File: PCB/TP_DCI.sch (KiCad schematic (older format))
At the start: 56 parts, among them K1 G5V-2-5DC, K2 G5V-2-5DC, P1 Conn_02x20, P2 Conn_02x20, Q1 BC817W, Q2 BC817W, U1 PS2805-4, U2 ACS725xLCTR-10AU, U3 PS2805-4, U4 ACS725xLCTR-10AU, U5 24AA1025, U6 DS3231

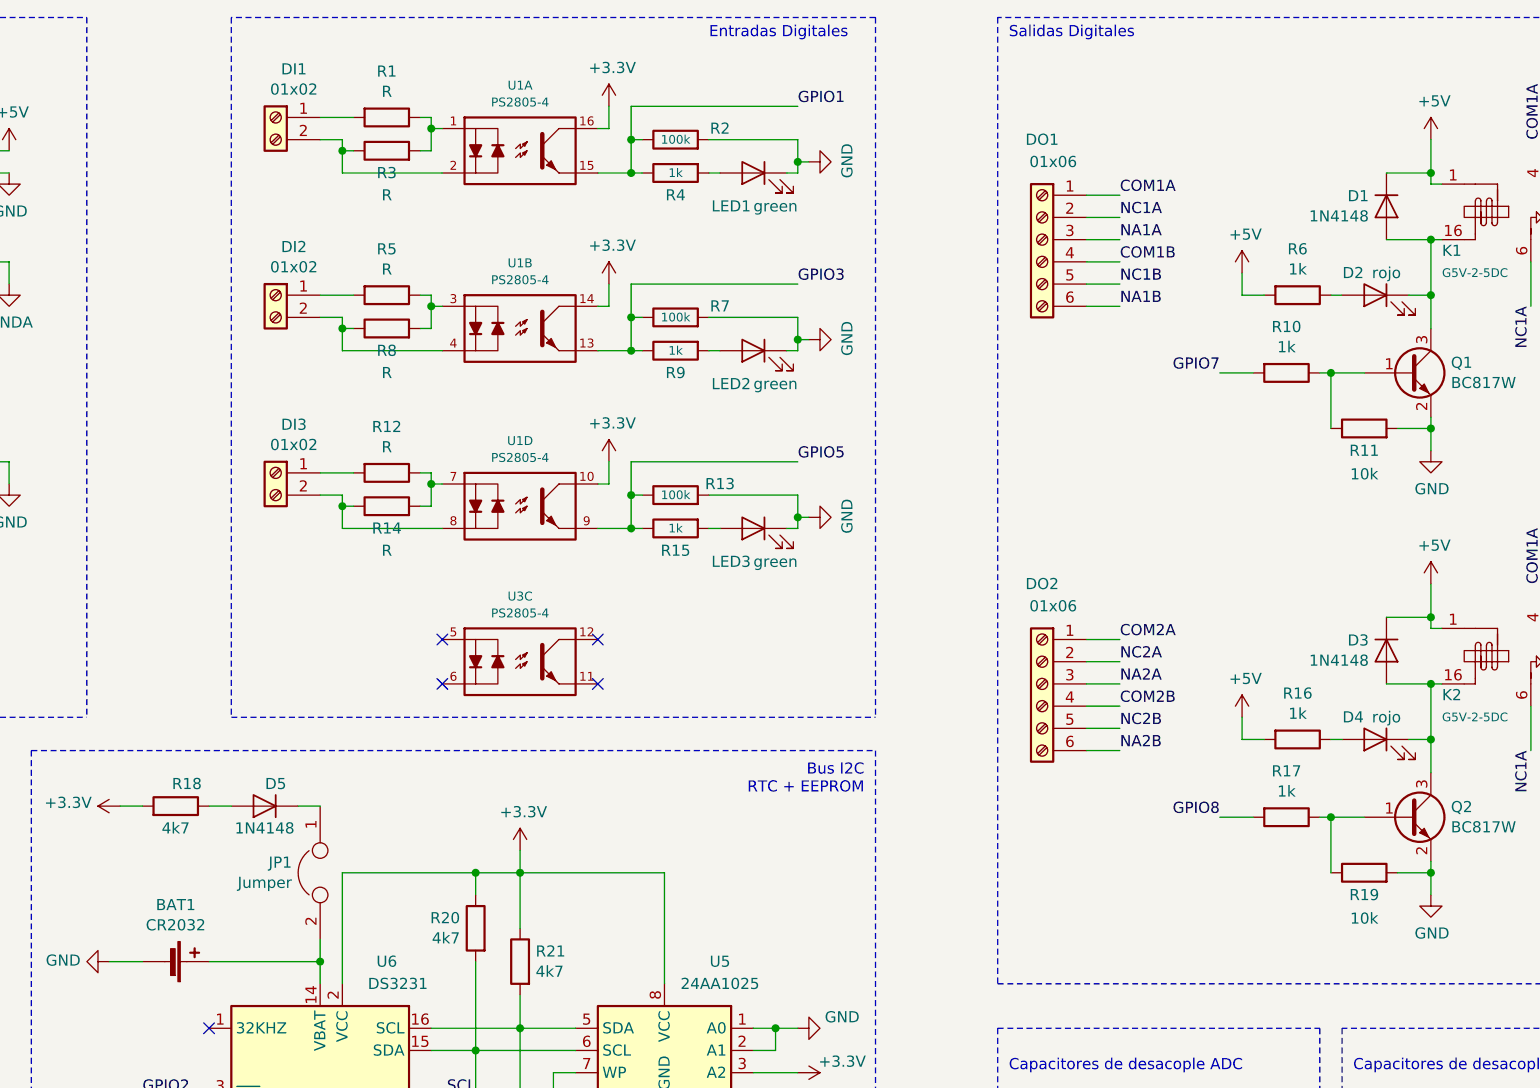
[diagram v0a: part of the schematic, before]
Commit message: correccion de footprints
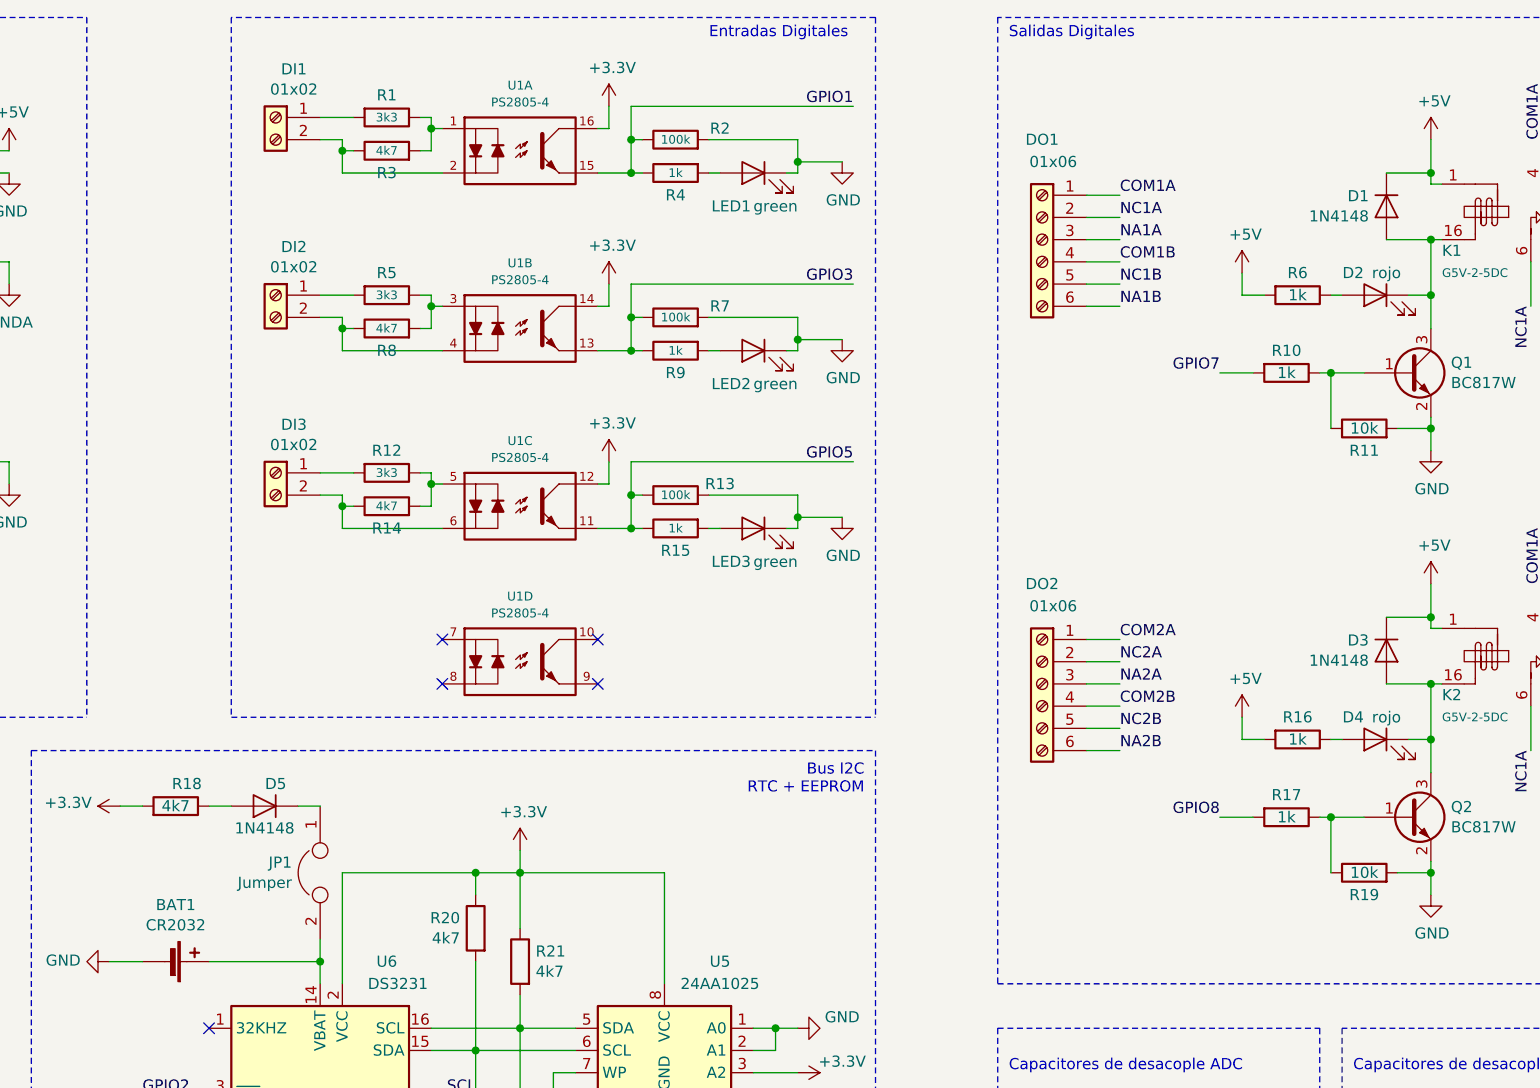
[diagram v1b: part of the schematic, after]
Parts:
- DO1, DO2: footprint (none) -> TerminalBlock:TerminalBlock_bornier-6_P5.08mm
- P1, P2: footprint Connector_IDC:IDC-Header_2x20_P2.54mm_Horizontal -> Connector_PinHeader_1.27mm:PinHeader_2x20_P1.27mm_Vertical
- R1, R12, R5: value R -> 3k3; footprint (none) -> Resistor_SMD:R_0805_2012Metric
- R10, R11, R13, R15, R16, R17, R18, R19, R2, R20, R21, R4, R6, R7, R9: footprint (none) -> Resistor_SMD:R_0805_2012Metric
- R14, R3, R8: value R -> 4k7; footprint (none) -> Resistor_SMD:R_0805_2012Metric
- U1: footprint SSOP-16 -> Package_SO:SOP-16_4.4x10.4mm_P1.27mm
- U1: renamed from U3; footprint SSOP-16 -> Package_SO:SOP-16_4.4x10.4mm_P1.27mm
- U5: footprint (none) -> Package_SO:SOIC-8_5.23x5.23mm_P1.27mm
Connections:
- net +3V3: now also U1.12; no longer U1.10
- net GPIO5: now also U1.11; no longer U1.9
- net at DI3.2 (Pin_2), R14.1: now also U1.6; no longer U1.8
- net at R12.1, R14.2: now also U1.5; no longer U1.7

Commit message: Se incorpora plantilla de poncho EDU-CIAA
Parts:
- DO2: footprint TerminalBlock:TerminalBlock_bornier-6_P5.08mm -> Connector_PinHeader_2.54mm:PinHeader_2x03_P2.54mm_Vertical; symbol Connector:Screw_Terminal_01x06 -> Connector_Generic:Conn_02x03_Odd_Even
- P1, P2: footprint Connector_PinHeader_1.27mm:PinHeader_2x20_P1.27mm_Vertical -> Connector_PinHeader_2.54mm:PinHeader_2x20_P2.54mm_Vertical
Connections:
- net COM1B: now also DO2.4 (Pin_4); no longer DO1.4 (Pin_4)
- net COM2A: now also DO1.4 (Pin_4); no longer DO2.1 (Pin_1)
- net COM2B: now also DO2.1 (Pin_1); no longer DO2.4 (Pin_4)
- net NA1B: now also DO2.6 (Pin_6); no longer DO1.6 (Pin_6)
- net NA2A: now also DO1.6 (Pin_6); no longer DO2.3 (Pin_3)
- net NA2B: now also DO2.3 (Pin_3); no longer DO2.6 (Pin_6)
- net NC1B: now also DO2.5 (Pin_5); no longer DO1.5 (Pin_5)
- net NC2A: now also DO1.5 (Pin_5); no longer DO2.2 (Pin_2)
- net NC2B: now also DO2.2 (Pin_2); no longer DO2.5 (Pin_5)
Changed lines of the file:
@@
 Wire Wire Line
 	8400 1750 8550 1750
+Text Label 8350 3100 2    50   ~ 0
+COM1B
+Wire Wire Line
+	8400 1850 8550 1850
+Text Label 9150 3200 0    50   ~ 0
+NC1B
+Wire Wire Line
+	8400 1950 8550 1950
+Text Label 8350 3200 2    50   ~ 0
+NA1B
 Text Label 8550 1750 0    50   ~ 0
-COM1B
-Wire Wire Line
-	8400 1850 8550 1850
+COM2A
+Wire Wire Line
+	8350 3100 8500 3100
 Text Label 8550 1850 0    50   ~ 0
-NC1B
-Wire Wire Line
-	8400 1950 8550 1950
+NC2A
+Wire Wire Line
+	8350 3200 8500 3200
 Text Label 8550 1950 0    50   ~ 0
-NA1B
-Wire Wire Line
-	8400 3450 8550 3450
-Text Label 8550 3450 0    50   ~ 0
-COM2A
-Wire Wire Line
-	8400 3550 8550 3550
-Text Label 8550 3550 0    50   ~ 0
-NC2A
-Wire Wire Line
-	8400 3650 8550 3650
-Text Label 8550 3650 0    50   ~ 0
 NA2A
 Wire Wire Line
-	8400 3750 8550 3750
-Text Label 8550 3750 0    50   ~ 0
+	9000 3000 9150 3000
+Text Label 9150 3000 0    50   ~ 0
 COM2B
 Wire Wire Line
-	8400 3850 8550 3850
-Text Label 8550 3850 0    50   ~ 0
+	9000 3100 9150 3100
+Text Label 8350 3000 2    50   ~ 0
 NC2B
 Wire Wire Line
-	8400 3950 8550 3950
-Text Label 8550 3950 0    50   ~ 0
+	9000 3200 9150 3200
+Text Label 9150 3100 0    50   ~ 0
 NA2B
 Wire Wire Line
@@
 	9950 1350 9950 1400
 $Comp
-L Connector:Screw_Terminal_01x06 DO2
+L Connector_Generic:Conn_02x03_Odd_Even DO2
 U 1 1 61C48A0E
-P 8200 3650
-F 0 "DO2" H 8200 4100 50  0000 C CNN
-F 1 "01x06" H 8150 4000 50  0000 C CNN
-F 2 "TerminalBlock:TerminalBlock_bornier-6_P5.08mm" H 8200 3650 50  0001 C CNN
-F 3 "~" H 8200 3650 50  0001 C CNN
-	1    8200 3650
+P 8800 3100
+F 0 "DO2" H 8850 3417 50  0000 C CNN
+F 1 "01x06" H 8850 3326 50  0000 C CNN
+F 2 "Connector_PinHeader_2.54mm:PinHeader_2x03_P2.54mm_Vertical" H 8800 3100 50  0001 C CNN
+F 3 "~" H 8800 3100 50  0001 C CNN
+	1    8800 3100
 	-1   0    0    -1
 $EndComp
@@
 F 0 "P1" H 1450 3267 50  0000 C CNN
 F 1 "Conn_02x20" H 1450 3176 50  0000 C CNN
-F 2 "Connector_PinHeader_1.27mm:PinHeader_2x20_P1.27mm_Vertical" H 1400 2150 50  0001 C CNN
+F 2 "Connector_PinHeader_2.54mm:PinHeader_2x20_P2.54mm_Vertical" H 1400 2150 50  0001 C CNN
 F 3 "~" H 1400 2150 50  0001 C CNN
 	1    1400 2150
@@
 F 0 "P2" H 2950 3267 50  0000 C CNN
 F 1 "Conn_02x20" H 2950 3176 50  0000 C CNN
-F 2 "Connector_PinHeader_1.27mm:PinHeader_2x20_P1.27mm_Vertical" H 2900 2150 50  0001 C CNN
+F 2 "Connector_PinHeader_2.54mm:PinHeader_2x20_P2.54mm_Vertical" H 2900 2150 50  0001 C CNN
 F 3 "~" H 2900 2150 50  0001 C CNN
 	1    2900 2150
@@
 Wire Wire Line
 	7100 2900 7100 2950
+Wire Wire Line
+	8350 3000 8500 3000
 $EndSCHEMATC

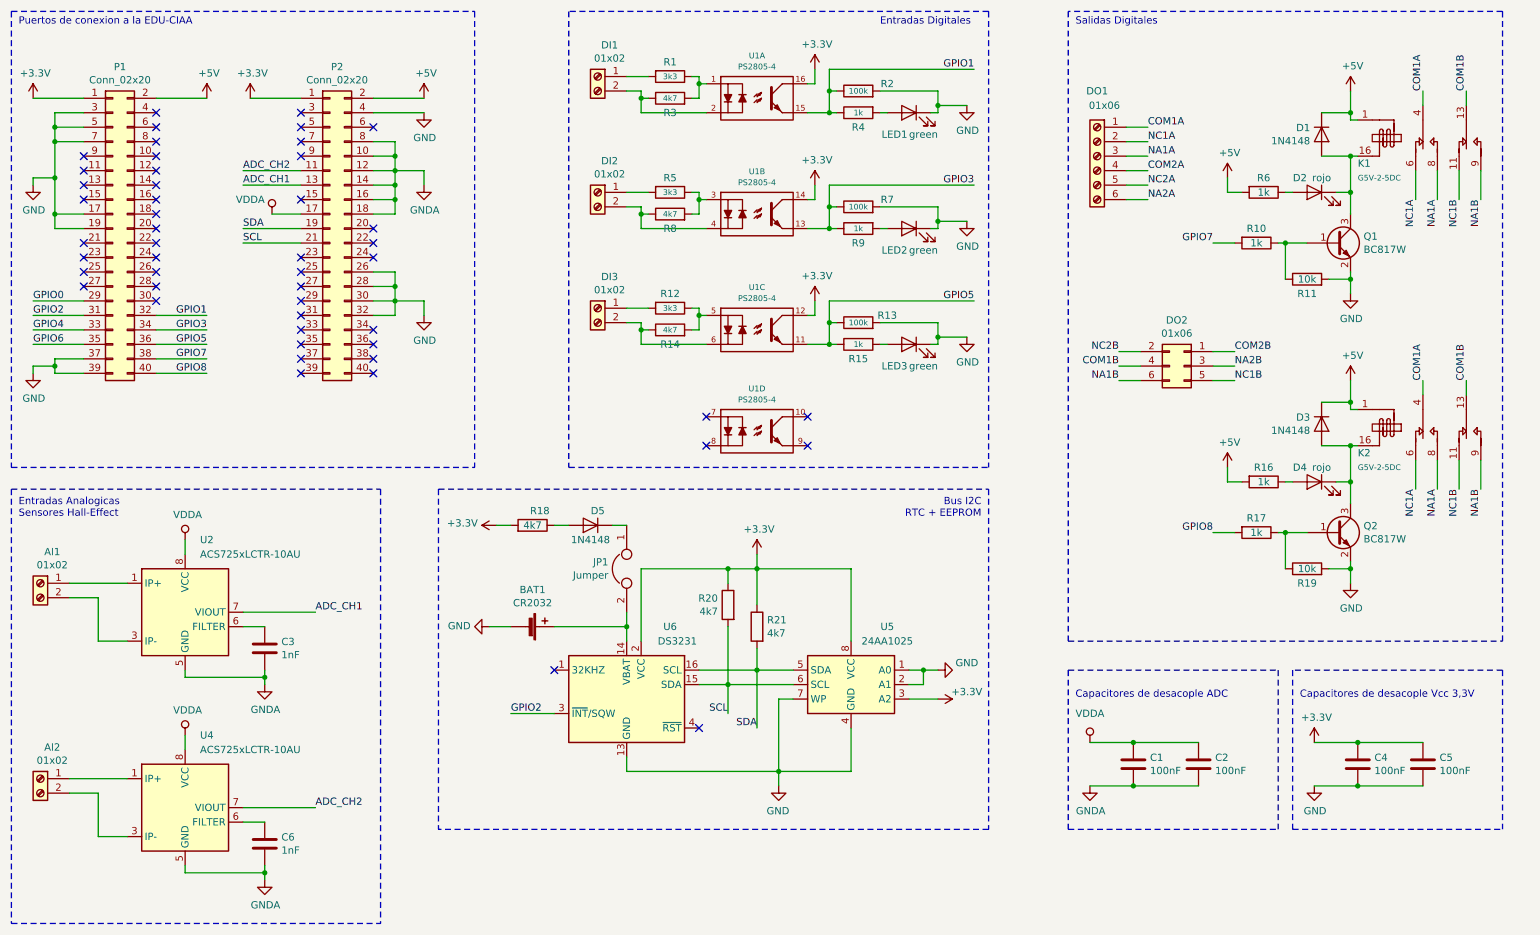
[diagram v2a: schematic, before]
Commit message: actualizacion de footprints y 3Dshapes
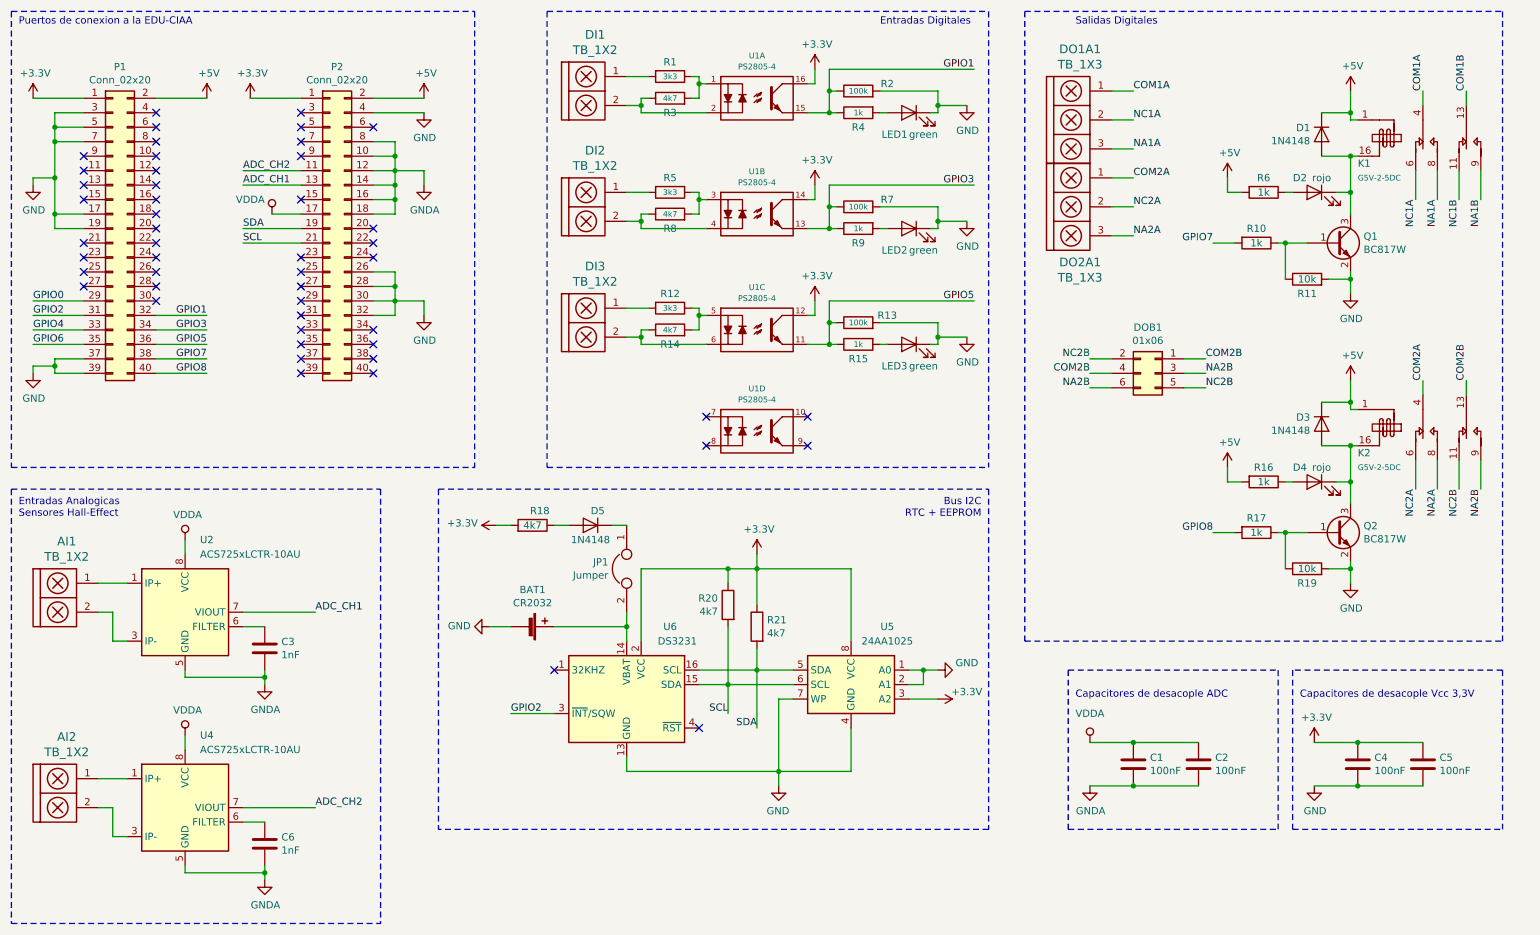
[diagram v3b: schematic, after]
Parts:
- removed AI1, AI2, DI1, DI2, DI3: 01x02, TerminalBlock:TerminalBlock_bornier-2_P5.08mm, symbol Connector:Screw_Terminal_01x02
- removed DO1: 01x06, TerminalBlock:TerminalBlock_bornier-6_P5.08mm, symbol Connector:Screw_Terminal_01x06
- added AI1, AI2, DI1, DI2, DI3: TB_1X2, Libreria_EDU_CIAA_NXP:bornier2, symbol w_device:TB_1X2
- added DO1A1, DO2A1: TB_1X3, Libreria_EDU_CIAA_NXP:bornier3, symbol w_device:TB_1X3
- C1, C2, C3, C4, C5, C6: footprint Capacitor_SMD:C_0201_0603Metric -> Capacitor_SMD:C_0805_2012Metric
- D1, D3, D5: footprint Diode_SMD:D_0603_1608Metric -> Diode_SMD:D_1206_3216Metric
- D2, D4: footprint LED_SMD:LED_0201_0603Metric -> LED_SMD:LED_0805_2012Metric
- renumbered DO2 to DOB1
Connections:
- net COM1A: now also DO1A1.1; no longer K2.4
- net COM1B: no longer DOB1.4 (Pin_4), K2.13
- net COM2A: now also K2.4, DO2A1.1
- net COM2B: now also DOB1.4 (Pin_4), K2.13
- net NA1A: now also DO1A1.3; no longer K2.8
- net NA1B: no longer DOB1.6 (Pin_6), K2.9
- net NA2A: now also K2.8, DO2A1.3
- net NA2B: now also DOB1.6 (Pin_6), K2.9
- net NC1A: now also DO1A1.2; no longer K2.6
- net NC1B: no longer DOB1.5 (Pin_5), K2.11
- net NC2A: now also K2.6, DO2A1.2
- net NC2B: now also DOB1.5 (Pin_5), K2.11
- net at R3.1, U1.2: now also DI1.2
- net at U2.1 (IP+), U2.2 (IP+): now also AI1.1
- net at U2.3 (IP-), U2.4 (IP-): now also AI1.2
- net at R1.2: now also DI1.1
- net at R5.2: now also DI2.1
- net at R8.1, U1.4: now also DI2.2
- net at R12.2: now also DI3.1
- net at R14.1, U1.6: now also DI3.2
- net at U4.1 (IP+), U4.2 (IP+): now also AI2.1
- net at U4.3 (IP-), U4.4 (IP-): now also AI2.2
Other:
- moved on the sheet: DOB1
